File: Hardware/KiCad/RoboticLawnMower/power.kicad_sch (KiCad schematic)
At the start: 6 parts, among them U6 LT1129-3.3_SOT223, U7 TSR_1-2450

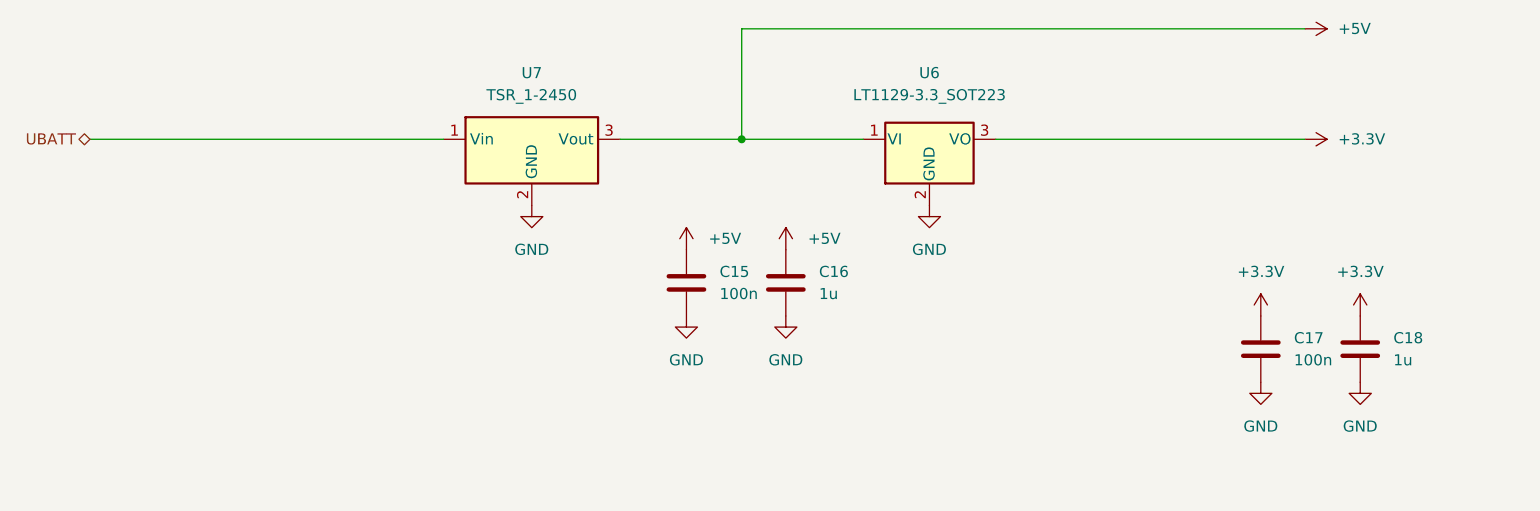
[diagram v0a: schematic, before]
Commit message: Redesign: - Controller - I2C pinning geändert - uvm
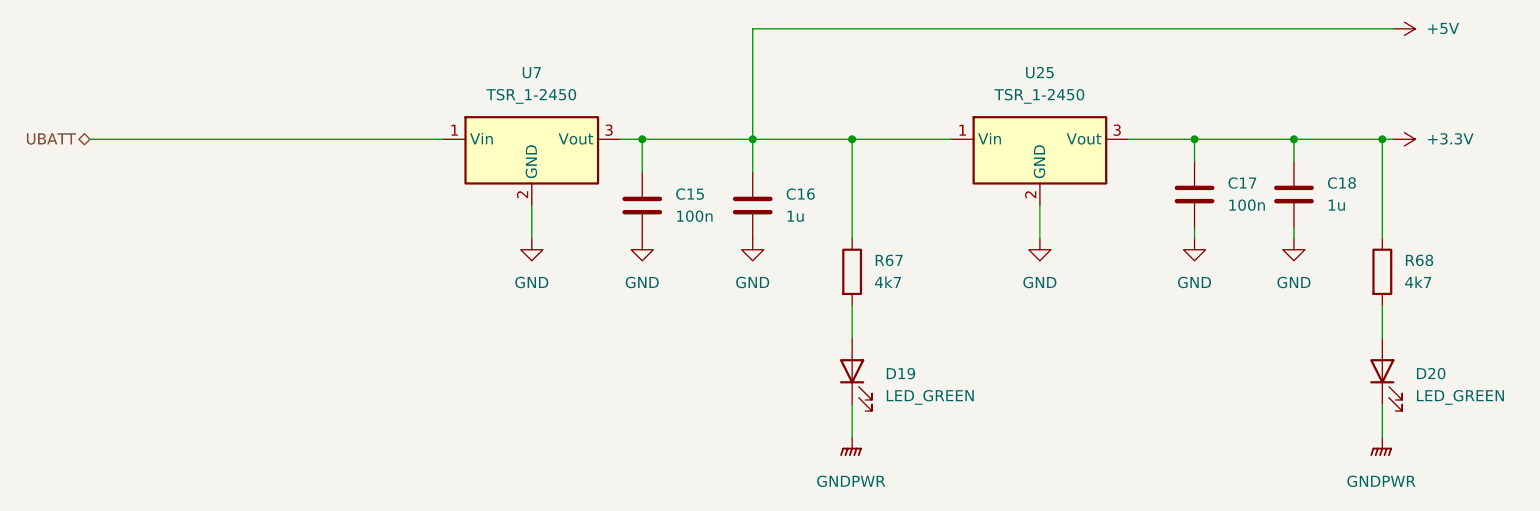
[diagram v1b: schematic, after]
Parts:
- removed U6: LT1129-3.3_SOT223, Package_TO_SOT_SMD:SOT-223-3_TabPin2, symbol Regulator_Linear:LT1129-3.3_SOT223
- added D19, D20: LED_GREEN, LED_SMD:LED_0603_1608Metric, symbol Device:LED
- added R67, R68: 4k7, Resistor_SMD:R_0603_1608Metric, symbol Device:R
- added U25: TSR_1-2450, Converter_DCDC:Converter_DCDC_TRACO_TSR-1_THT, symbol Regulator_Switching:TSR_1-2450
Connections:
- net +3.3V: now also R68.1, U25.3 (Vout)
- net +5V: now also R67.1, U25.1 (Vin)
- net GND: now also U25.2 (GND)
- new net: D20.2 (A), R68.2
- new net: D19.2 (A), R67.2
- new net GNDPWR: D19.1 (K), D20.1 (K)
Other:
- moved on the sheet: C15, C16, C17, C18
